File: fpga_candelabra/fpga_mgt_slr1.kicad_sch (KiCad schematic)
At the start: 1 part, among them U1 XCVU13P-B2104

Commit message: candelabra: add i-pex extension ports, remove FMC1
* update bank/mgt allocation
* add basic pcb floorplanning

Signed-off-by: Yichuan Gao <gaoyichuan000@gmail.com>
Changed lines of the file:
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@@
+		)
+	)
+	(bus
+		(pts
+			(xy 262.89 156.21) (xy 280.67 156.21)
+		)
+		(stroke
+			(width 0)
+			(type default)
 		)
 	)
@@
 		)
 	)
+	(label "FMC0{FMC_HPC}"
+		(at 264.16 156.21 0)
+		(fields_autoplaced yes)
+		(effects
+			(font
+				(size 1.27 1.27)
+			)
+			(justify left bottom)
+		)
+	)
 	(label "PCIE.PER14+"
 		(at 19.05 143.51 0)
@@
 		(fields_autoplaced yes)
 		(effects
+			(font
+				(size 1.27 1.27)
+			)
+			(justify right)
+		)
+	)
+	(hierarchical_label "FMC0{FMC_HPC}"
+		(shape bidirectional)
+		(at 262.89 156.21 180)
+		(fields_autoplaced yes)
+		(effects

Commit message: fpga_candelabra: major revision
* Finish DDR4 & QSFP+ & PCIe layout
* Change FMC to LPC
* Add mikroBUS extension
* 12V input & PDN updates
* FPGA config updates

Signed-off-by: Yichuan Gao <gaoyichuan000@gmail.com>
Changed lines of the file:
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@@
 		)
 	)
-	(label "FMC0{FMC_HPC}"
+	(label "FMC0{FMC_LPC}"
 		(at 264.16 156.21 0)
 		(fields_autoplaced yes)
@@
 		)
 	)
-	(hierarchical_label "FMC0{FMC_HPC}"
+	(hierarchical_label "FMC0{FMC_LPC}"
 		(shape bidirectional)
 		(at 262.89 156.21 180)

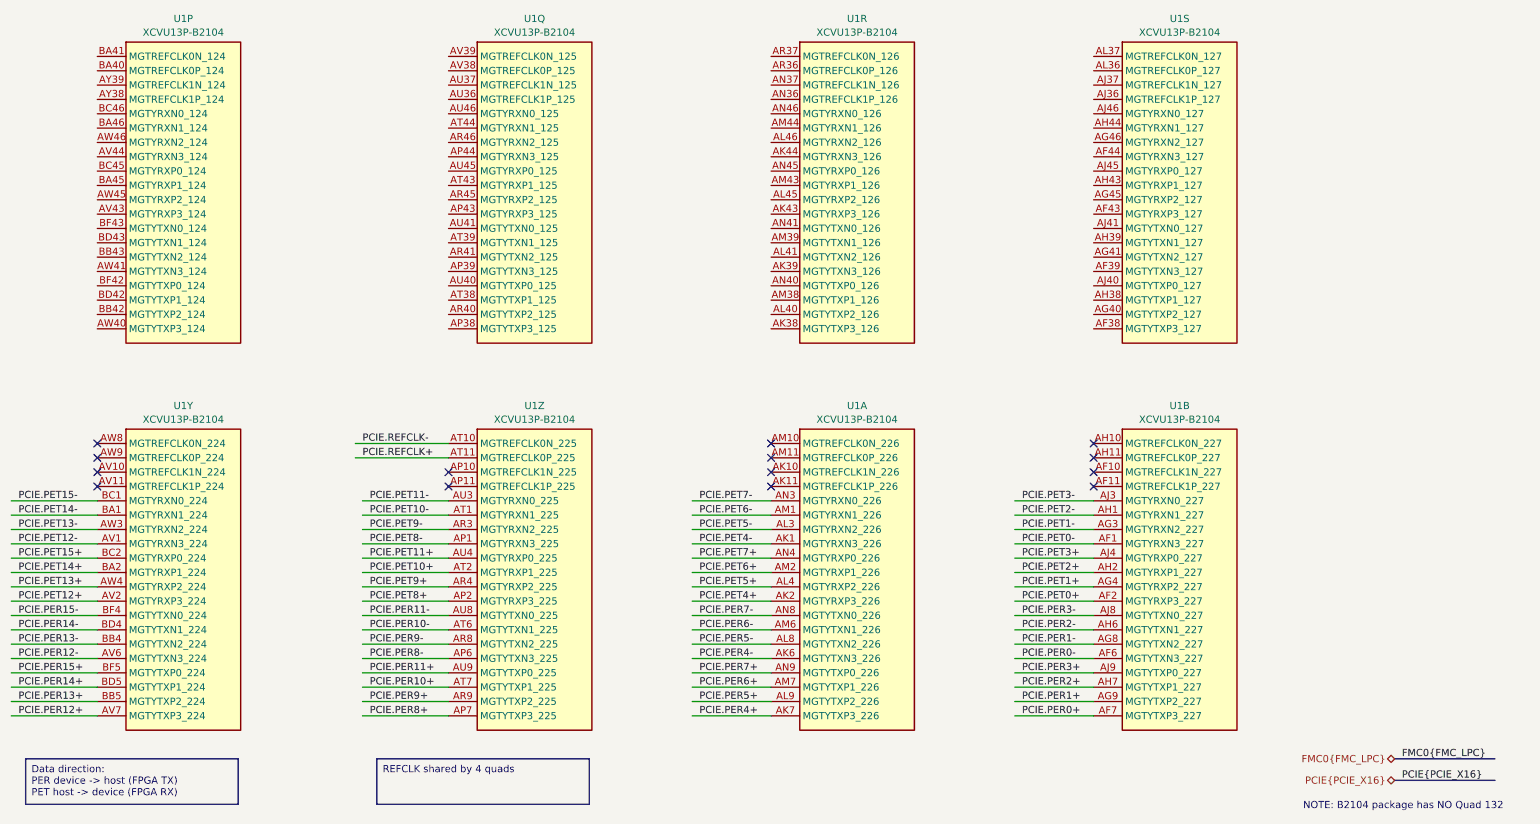
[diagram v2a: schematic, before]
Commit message: fpga_candelabra: sch & layout v0.5, pass basic ERC & DRC
Signed-off-by: Yichuan Gao <gaoyichuan000@gmail.com>
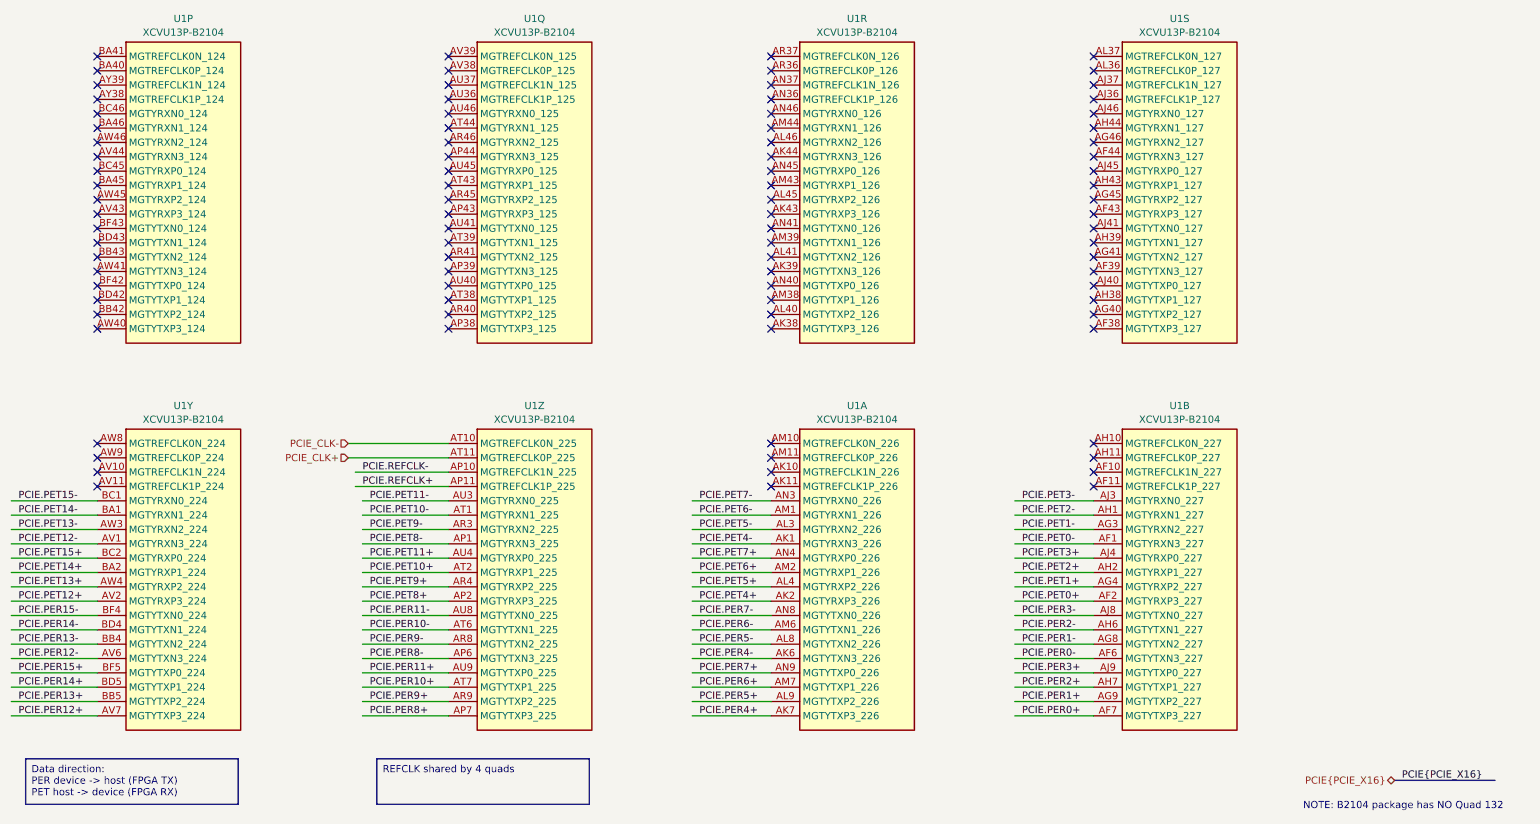
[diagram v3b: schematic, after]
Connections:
- net PCIE.REFCLK+: now also U1.AP11 (MGTREFCLK1P_225); no longer U1.AT11 (MGTREFCLK0P_225)
- net PCIE.REFCLK-: now also U1.AP10 (MGTREFCLK1N_225); no longer U1.AT10 (MGTREFCLK0N_225)
- new net PCIE_CLK+: U1.AT11 (MGTREFCLK0P_225)
- new net PCIE_CLK-: U1.AT10 (MGTREFCLK0N_225)
- no-connect marks 14 -> 92

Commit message: fpga_candelabra: add author & rev to schematics
Signed-off-by: Yichuan Gao <gaoyichuan000@gmail.com>
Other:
- company: (none) -> CHIPS Alliance
- title: (none) -> FPGA SLR1 MGT
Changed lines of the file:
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@@
 	(generator_version "8.0")
 	(paper "A4")
+	(title_block
+		(title "FPGA SLR1 MGT")
+		(date "2025-02-05")
+		(rev "0.2.0")
+		(company "CHIPS Alliance")
+		(comment 1 "Yichuan Gao")
+		(comment 2 "Yichuan Gao")
+	)
 	(no_connect
 		(at 209.55 39.37)

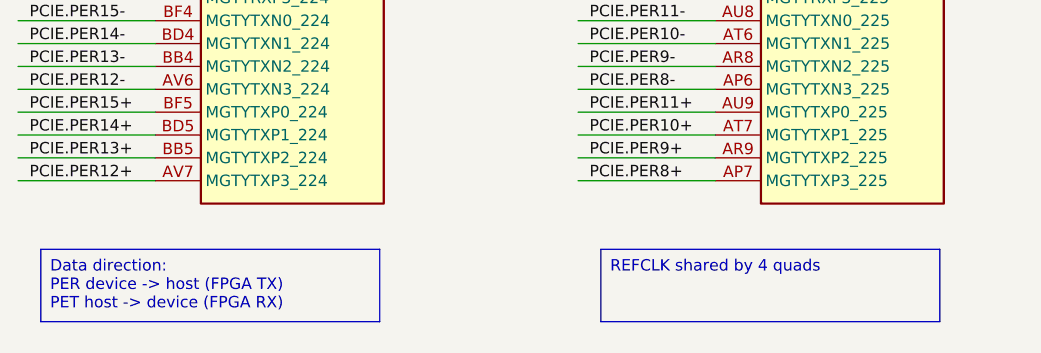
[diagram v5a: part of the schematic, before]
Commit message: fpga_candelabra: update to kicad 9.0
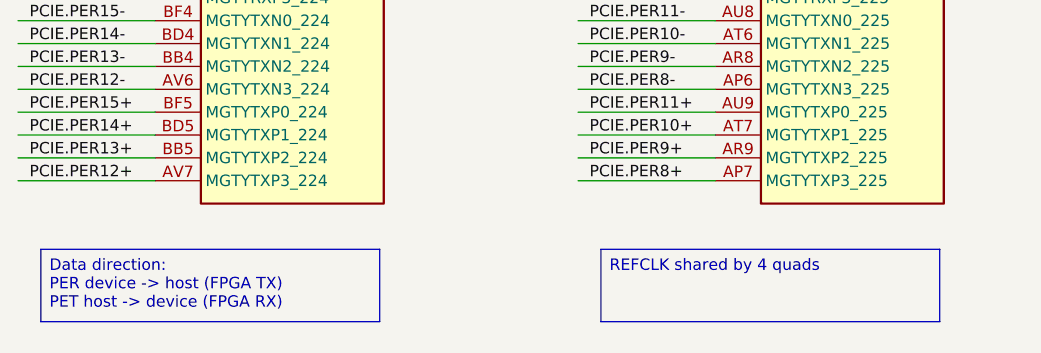
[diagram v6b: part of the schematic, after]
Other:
- company: CHIPS Alliance -> Sipeed
